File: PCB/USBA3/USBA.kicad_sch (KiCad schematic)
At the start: 20 parts, among them J1 USB_A, U1 ESP32-PICO-MINI-02, U2 LMR16006YDDCR, U3 CH340X, U4 QR

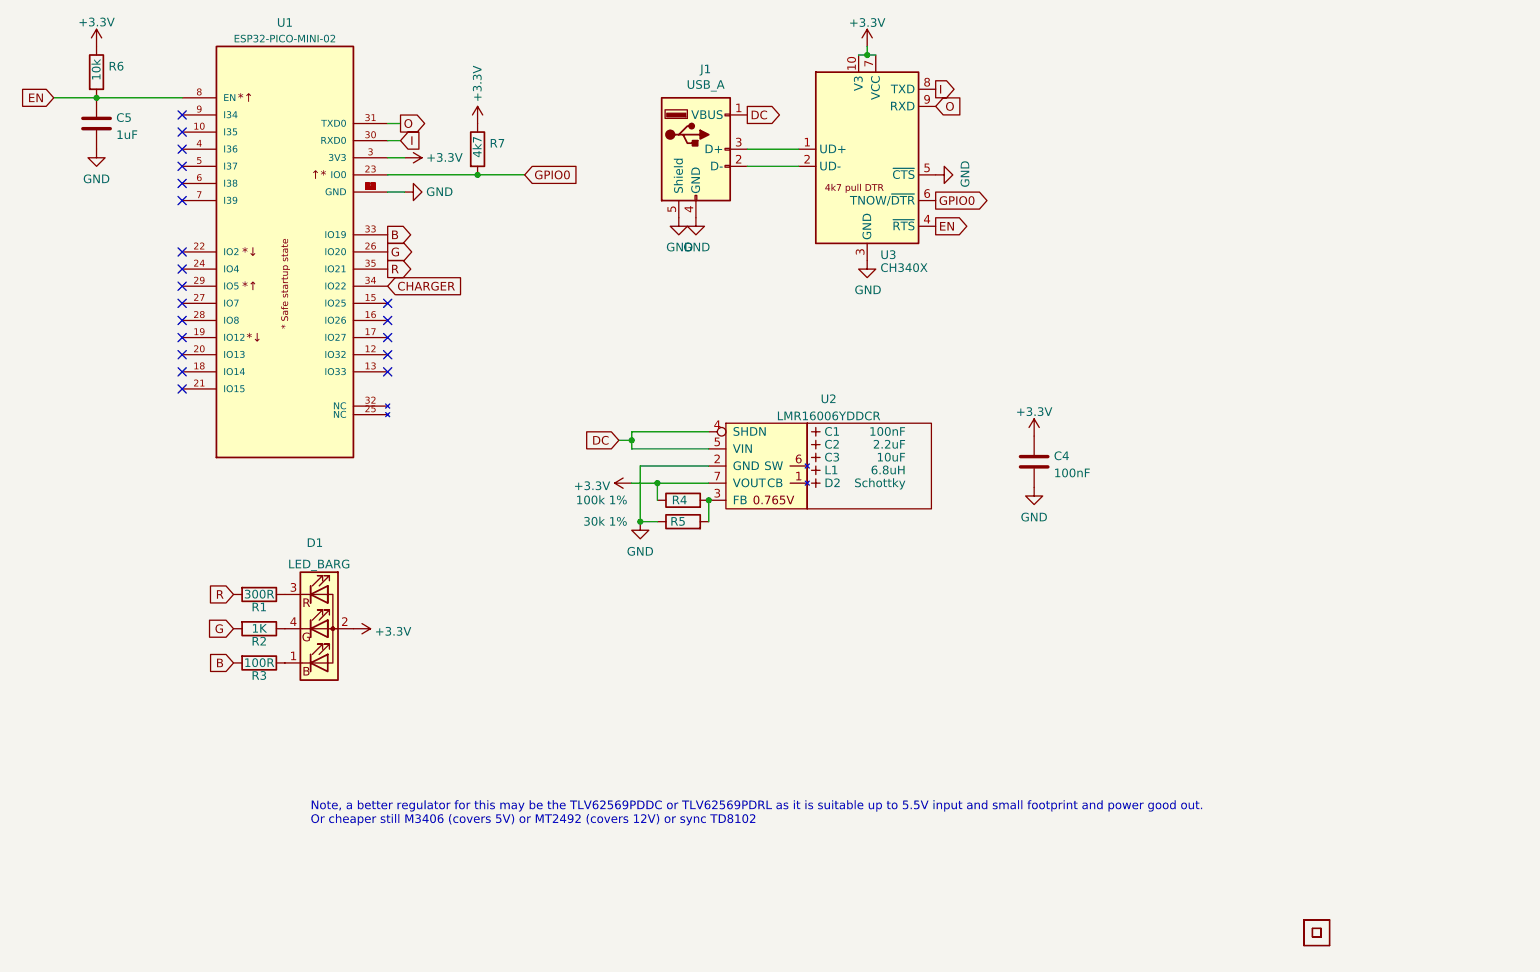
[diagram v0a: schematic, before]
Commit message: New regulator
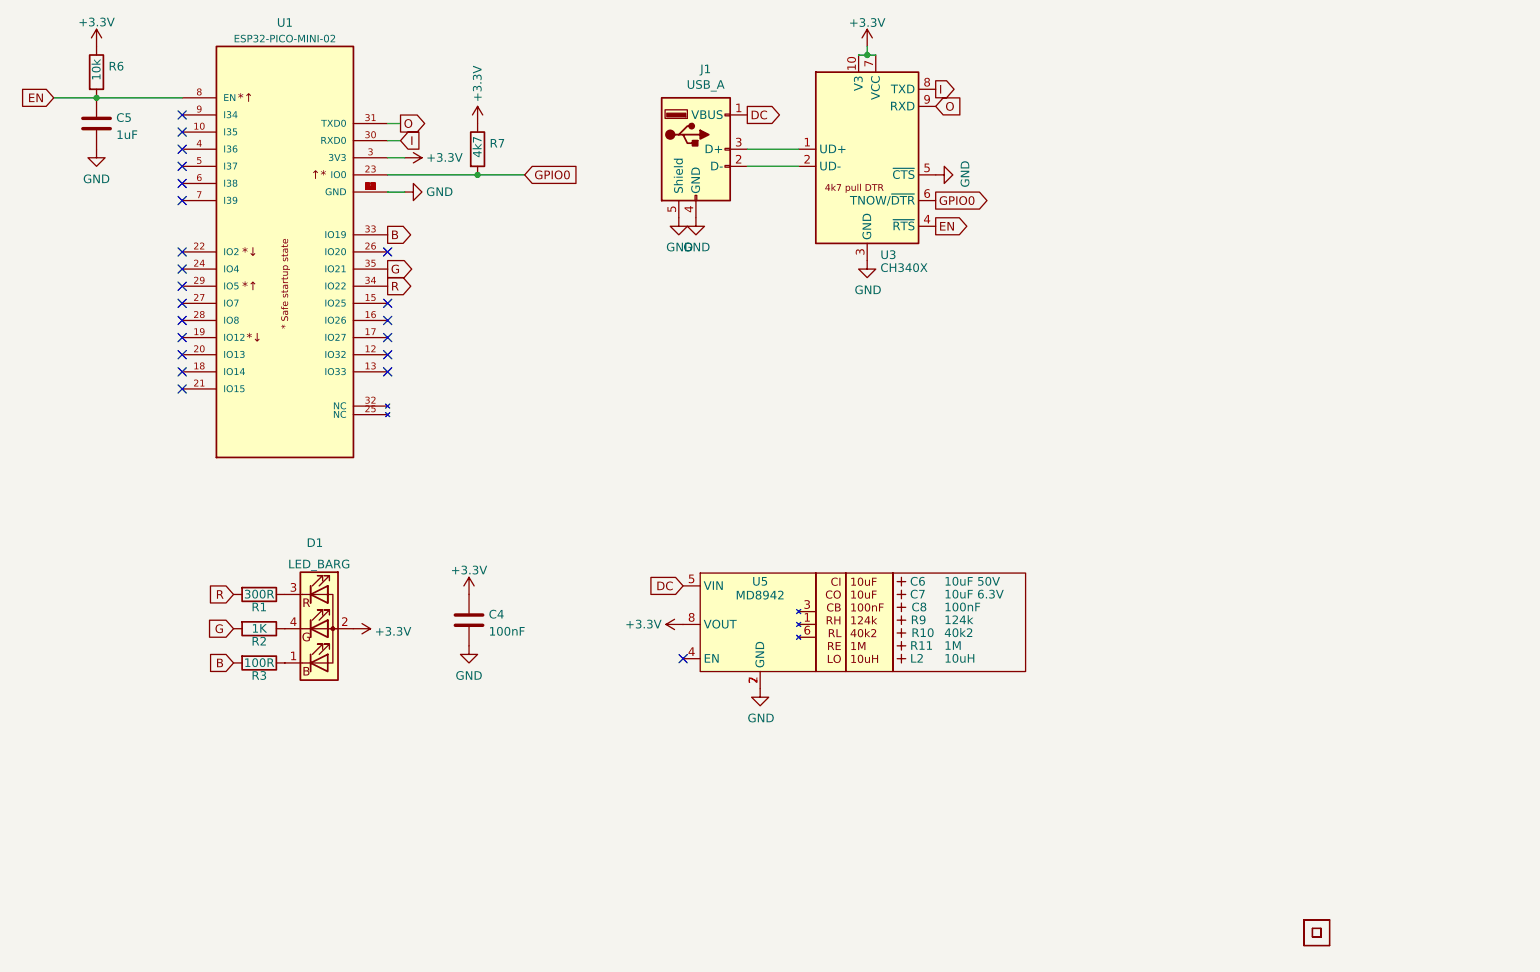
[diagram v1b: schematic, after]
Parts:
- removed C1: 100nF, RevK:C_0603_, symbol RevK:Hidden
- removed C2: 2.2uF, RevK:C_0805_, symbol RevK:Hidden
- removed C3: 10uF, RevK:C_0805_, symbol RevK:Hidden
- removed D2: Schottky, RevK:D_1206_, symbol RevK:Hidden
- removed L1: 6.8uH, RevK:L_4x4_, symbol RevK:Hidden
- removed R4: 100k 1%, RevK:R_0603, symbol Device:R
- removed R5: 30k 1%, RevK:R_0603, symbol Device:R
- removed U2: LMR16006YDDCR, RevK:SOT-23-Thin-6-Reg, symbol RevK:LMR16006XDDCR
- added C6: 10uF 50V, RevK:C_0603_, symbol RevK:Hidden
- added C7: 10uF 6.3V, RevK:C_0603_, symbol RevK:Hidden
- added C8: 100nF, RevK:C_0603_, symbol RevK:Hidden
- added L2: 10uH, RevK:L_4x4_, symbol RevK:Hidden
- added R10: 40k2, RevK:R_0402_, symbol RevK:Hidden
- added R11: 1M, RevK:R_0402_, symbol RevK:Hidden
- added R9: 124k, RevK:R_0402_, symbol RevK:Hidden
- added U5: MD8942, RevK:SOT-23-6-MD8942, symbol RevK:MD89420-RegBlock
- C4: footprint RevK:C_0603 -> RevK:C_0402; Part No 0603-100nF-25V -> (none)
- C5: footprint RevK:C_0603 -> RevK:C_0402; Part No 0603-10nF-50V -> (none)
- R1: footprint RevK:R_0603 -> RevK:R_0402; Part No 0603-680R -> (none)
- R2: footprint RevK:R_0603 -> RevK:R_0402; Part No 0603-2K -> (none)
- R3: footprint RevK:R_0603 -> RevK:R_0402; Part No 0603-220R -> (none)
- R6, R7: footprint RevK:R_0603 -> RevK:R_0402
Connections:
- net CHARGER is gone; now on net R: U1.34 (IO22)
- net +3.3V: now also U5.8 (VOUT)
- net DC: now also U5.5 (VIN)
- net G: now also U1.35 (IO21); no longer U1.26 (IO20)
- net GND: now also U5.2 (GND), U5.7 (GND)
- net R: no longer U1.35 (IO21)
- no-connect marks 20 -> 22
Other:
- note removed: "Note, a better regulator for this may be the TLV62569PDDC or TLV62569PDRL as it is suitable up to 5.5V input and small footprint and power good out. Or cheaper still M3406 (covers 5V) or MT2492 (covers 12V) or sync TD8102"
- moved on the sheet: C4

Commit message: Smaller
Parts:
- removed R7: 4k7, RevK:R_0402, symbol Device:R
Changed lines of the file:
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@@
   (junction (at 193.04 43.18) (diameter 0) (color 0 0 0 0)
-  )
-  (junction (at 135.255 60.96) (diameter 0) (color 0 0 0 0)
   )
   (junction (at 78.74 49.53) (diameter 0) (color 0 0 0 0)
@@
   (no_connect (at 121.92 72.39))
   (no_connect (at 91.44 72.39))
-  (wire (pts (xy 121.92 60.96) (xy 135.255 60.96))
-    (stroke (width 0) (type default))
-  )
   (wire (pts (xy 121.92 63.5) (xy 124.46 63.5))
     (stroke (width 0) (type default))
   )
   (wire (pts (xy 121.92 58.42) (xy 124.46 58.42))
-    (stroke (width 0) (type default))
-  )
-  (wire (pts (xy 135.255 60.96) (xy 142.24 60.96))
     (stroke (width 0) (type default))
   )
@@
     )
   )
-  (global_label "GPIO0" (shape input) (at 142.24 60.96 0) (fields_autoplaced)
-    (effects (font (size 1.27 1.27)) (justify left))
-    (property "Intersheetrefs" "${INTERSHEET_REFS}" (at 61.595 24.13 0)
+  (global_label "GPIO0" (shape input) (at 121.92 60.96 0) (fields_autoplaced)
+    (effects (font (size 1.27 1.27)) (justify left))
+    (property "Intersheetrefs" "${INTERSHEET_REFS}" (at 41.275 24.13 0)
       (effects (font (size 1.27 1.27)) hide)
     )
@@
         (path "/babeabf2-f3b0-4ed5-8d9e-0215947e6cf3"
           (reference "C6") (unit 1)
-        )
-      )
-    )
-  )
-  (symbol (lib_id "power:+3.3V") (at 135.255 53.34 0) (unit 1)
-    (in_bom yes) (on_board yes) (dnp no)
-    (property "Reference" "#PWR04" (at 135.255 57.15 0)
-      (effects (font (size 1.27 1.27)) hide)
-    )
-    (property "Value" "+3.3V" (at 135.255 50.165 90)
-      (effects (font (size 1.27 1.27)) (justify left))
-    )
-    (property "Footprint" "" (at 135.255 53.34 0)
-      (effects (font (size 1.27 1.27)) hide)
-    )
-    (property "Datasheet" "" (at 135.255 53.34 0)
-      (effects (font (size 1.27 1.27)) hide)
-    )
-    (pin "1")
-    (instances
-      (project "USBA"
-        (path "/2d210a96-f81f-42a9-8bf4-1b43c11086f3"
-          (reference "#PWR04") (unit 1)
         )
       )
@@
         )
       )
-    )
-  )
-  (symbol (lib_id "Device:R") (at 135.255 57.15 0) (unit 1)
-    (in_bom yes) (on_board yes) (dnp no)
-    (property "Reference" "R7" (at 137.033 56.3153 0)
-      (effects (font (size 1.27 1.27)) (justify left))
-    )
-    (property "Value" "4k7" (at 135.255 58.42 90)
-      (effects (font (size 1.27 1.27)) (justify left))
-    )
-    (property "Footprint" "RevK:R_0402" (at 133.477 57.15 90)
-      (effects (font (size 1.27 1.27)) hide)
-    )
-    (property "Datasheet" "~" (at 135.255 57.15 0)
-      (effects (font (size 1.27 1.27)) hide)
-    )
-    (pin "1")
-    (pin "2")
-    (instances
-      (project "USBA"
-        (path "/2d210a96-f81f-42a9-8bf4-1b43c11086f3"
-          (reference "R7") (unit 1)
-        )
-      )

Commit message: Panel
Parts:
- added FID1, FID2, FID3, FID4, FID5, FID6, FID7, FID8: Fiducial, Fiducial:Fiducial_1mm_Mask2mm, symbol Mechanical:Fiducial
- added H1, H2, H3, H4: MountingHole, MountingHole:MountingHole_2mm, symbol Mechanical:MountingHole
- added U2, U6: Barcode, RevK:EAN-5060634238069, symbol RevK:Barcode

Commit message: Tidy
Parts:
- removed D1: LED_BARG, RevK:MHS190RGBCT, symbol Device:LED_BARG
- removed R1: 300R, RevK:R_0402, symbol Device:R
- removed R2: 1K, RevK:R_0402, symbol Device:R
- removed R3: 100R, RevK:R_0402, symbol Device:R
- added D2: RGB, RevK:LED-RGB-1.6x1.6, symbol Device:LED_RBGA
- added R4: 680R, RevK:R_0402, symbol Device:R
- added R5: 2K, RevK:R_0402, symbol Device:R
- added R7: 220R, RevK:R_0402, symbol Device:R
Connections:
- net +3.3V: now also D2.4 (A)
- net B: now also U1.35 (IO21), R7.2; no longer U1.33 (IO19)
- net G: now also U1.33 (IO19), R5.2; no longer U1.35 (IO21)
- net R: now also R4.2
- new net: D2.1 (RK), R4.1
- new net: D2.2 (BK), R7.1
- new net: D2.3 (GK), R5.1

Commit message: Re panel
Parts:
- removed H1, H2, H3, H4: MountingHole, MountingHole:MountingHole_2mm, symbol Mechanical:MountingHole
- removed U6: Barcode, RevK:EAN-5060634238069, symbol RevK:Barcode
- U4: footprint RevK:QR-GENERIC -> RevK:QR-USBA
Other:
- moved on the sheet: FID1, FID2, FID3, FID4, FID5, FID6, FID7, FID8

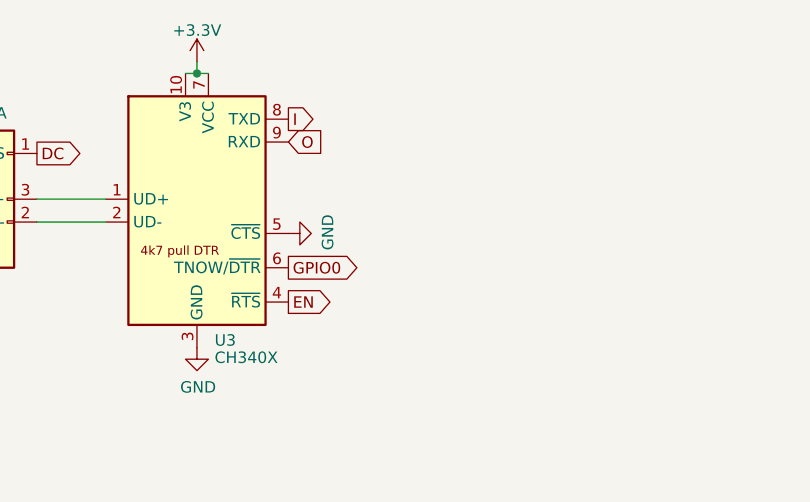
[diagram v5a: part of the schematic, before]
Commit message: FFS missing 4k7
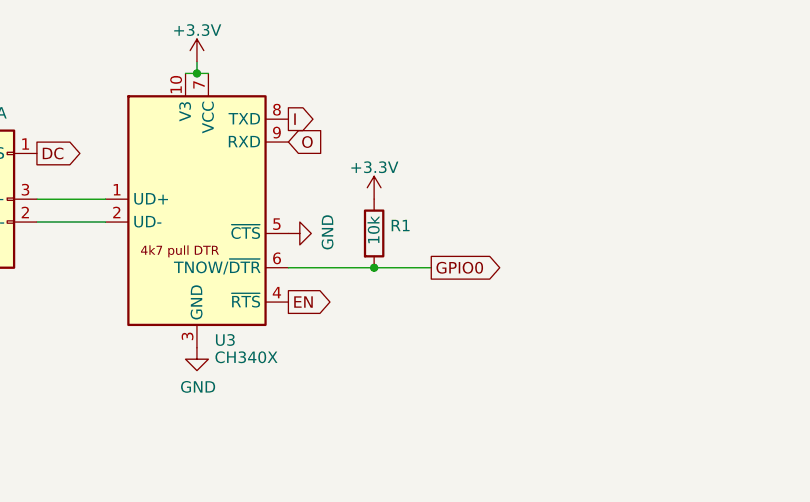
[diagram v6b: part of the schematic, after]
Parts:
- added R1: 10k, RevK:R_0402, symbol Device:R
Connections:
- net +3.3V: now also R1.1
- net GPIO0: now also R1.2
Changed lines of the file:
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@@
   (junction (at 193.04 43.18) (diameter 0) (color 0 0 0 0)
+  )
+  (junction (at 212.725 64.77) (diameter 0) (color 0 0 0 0)
   )
   (junction (at 78.74 49.53) (diameter 0) (color 0 0 0 0)
@@
     (stroke (width 0) (type default))
   )
+  (wire (pts (xy 203.2 64.77) (xy 212.725 64.77))
+    (stroke (width 0) (type default))
+  )
   (wire (pts (xy 121.92 58.42) (xy 124.46 58.42))
     (stroke (width 0) (type default))
@@
   )
   (wire (pts (xy 121.92 55.88) (xy 123.825 55.88))
+    (stroke (width 0) (type default))
+  )
+  (wire (pts (xy 212.725 64.77) (xy 219.075 64.77))
     (stroke (width 0) (type default))
   )
@@
     )
   )
-  (global_label "GPIO0" (shape output) (at 203.2 64.77 0) (fields_autoplaced)
+  (global_label "GPIO0" (shape output) (at 219.075 64.77 0) (fields_autoplaced)
     (effects (font (size 1.27 1.27)) (justify left))
-    (property "Intersheetrefs" "${INTERSHEET_REFS}" (at 211.1364 64.77 0)
+    (property "Intersheetrefs" "${INTERSHEET_REFS}" (at 227.0114 64.77 0)
       (effects (font (size 1.27 1.27)) (justify left) hide)
     )
@@
         (path "/46c350bb-7de4-4e81-aafd-4af55e37aab0"
           (reference "FID2") (unit 1)
+        )
+      )
+    )
+  )
+  (symbol (lib_id "Device:R") (at 212.725 60.96 0) (unit 1)
+    (in_bom yes) (on_board yes) (dnp no)
+    (property "Reference" "R1" (at 214.503 60.1253 0)
+      (effects (font (size 1.27 1.27)) (justify left))
+    )
+    (property "Value" "10k" (at 212.725 62.23 90)
+      (effects (font (size 1.27 1.27)) (justify left))
+    )
+    (property "Footprint" "RevK:R_0402" (at 210.947 60.96 90)
+      (effects (font (size 1.27 1.27)) hide)
+    )
+    (property "Datasheet" "~" (at 212.725 60.96 0)
+      (effects (font (size 1.27 1.27)) hide)
+    )
+    (pin "1")
+    (pin "2")
+    (instances
+      (project "USBA"
+        (path "/2d210a96-f81f-42a9-8bf4-1b43c11086f3"
+          (reference "R1") (unit 1)
         )
       )
@@
         )
       )
+    )
+  )
+  (symbol (lib_id "power:+3.3V") (at 212.725 57.15 0) (unit 1)
+    (in_bom yes) (on_board yes) (dnp no) (fields_autoplaced)
+    (property "Reference" "#PWR05" (at 212.725 60.96 0)
+      (effects (font (size 1.27 1.27)) hide)
+    )
+    (property "Value" "+3.3V" (at 212.725 53.6481 0)
+      (effects (font (size 1.27 1.27)))
+    )
+    (property "Footprint" "" (at 212.725 57.15 0)
+      (effects (font (size 1.27 1.27)) hide)
+    )
+    (property "Datasheet" "" (at 212.725 57.15 0)
+      (effects (font (size 1.27 1.27)) hide)
+    )
+    (pin "1")
+    (instances
+      (project "USBA"
+        (path "/2d210a96-f81f-42a9-8bf4-1b43c11086f3"
+          (reference "#PWR05") (unit 1)
+        )
+      )

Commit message: 4k7
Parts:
- R1: value 10k -> 4k7
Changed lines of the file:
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@@
       (effects (font (size 1.27 1.27)) (justify left))
     )
-    (property "Value" "10k" (at 212.725 62.23 90)
+    (property "Value" "4k7" (at 212.725 62.23 90)
       (effects (font (size 1.27 1.27)) (justify left))
     )
